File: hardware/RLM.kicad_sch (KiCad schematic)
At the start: 12 parts, among them U6 AP1117-33

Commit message: feat: add GY-521 footprint
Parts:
- U5: footprint (none) -> GRC:MicroSD-Module
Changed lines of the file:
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@@
       (effects (font (size 1.27 1.27)))
     )
-    (property "Footprint" "" (at 161.29 83.82 0)
+    (property "Footprint" "GRC:MicroSD-Module" (at 161.29 83.82 0)
       (effects (font (size 1.27 1.27)) hide)
     )

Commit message: chore: reorganize schematic
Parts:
- renumbered U6 to U3, U3 to U4, U4 to U5, U5 to U6
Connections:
- net +3.3V: no longer U6.2 (VCC)
- net +5V: now also U6.2 (VCC)
- net BN_RX: no longer U1.22 (TX2)
- net BN_TX: no longer U1.21 (RX2)
- net GY_SCL: no longer U1.29 (D22)
- net GY_SDA: no longer U1.26 (D21)
- net NRF_CE: no longer U1.20 (D4)
- net NRF_CSN: no longer U1.23 (D5)
- net NRF_MISO: no longer U1.25 (D19)
- net NRF_MOSI: no longer U1.30 (D23)
- net NRF_SCK: no longer U1.24 (D18)
- no-connect marks 8 -> 5
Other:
- note added: "Accelerometer/Gyroscope"
- note added: "ESP32 Pin Connections:"
- note added: "GPS"
- note added: "IMPORTANT: Before tracing, must finalize ESP32 pin connections TODO: - 2x 3-pin MOLEX - +5V, GND, V_sense - CAN_H, CAN_L, GND - CAN transciever"
- note added: "MicroSD Module"
- note added: "Microcontroller"
- note added: "Radio Module"
- note added: "Voltage Regulator"
- title: (none) -> Remote Logging Module
- moved on the sheet: C1, C2, C3, C4, D1, R1, U1, U2, U3, U4, U5, U6

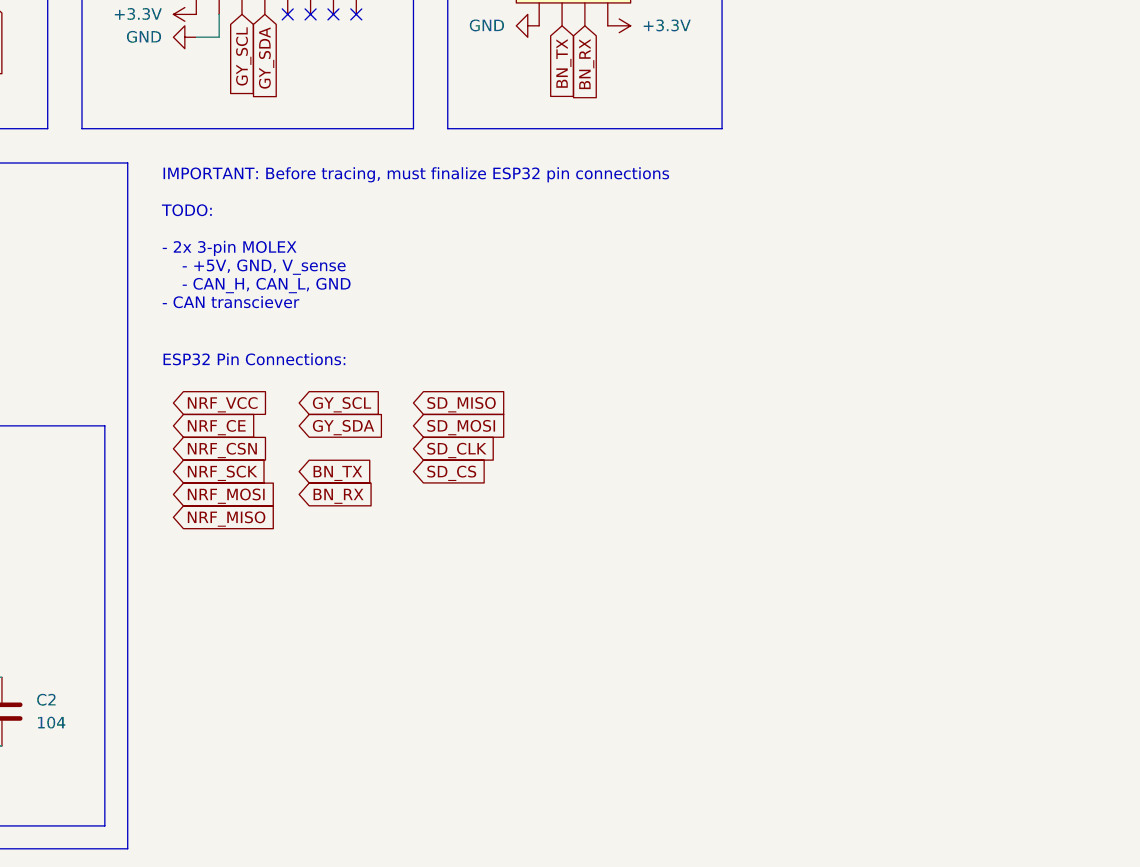
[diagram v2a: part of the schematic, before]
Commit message: feat: add CAN transceiver
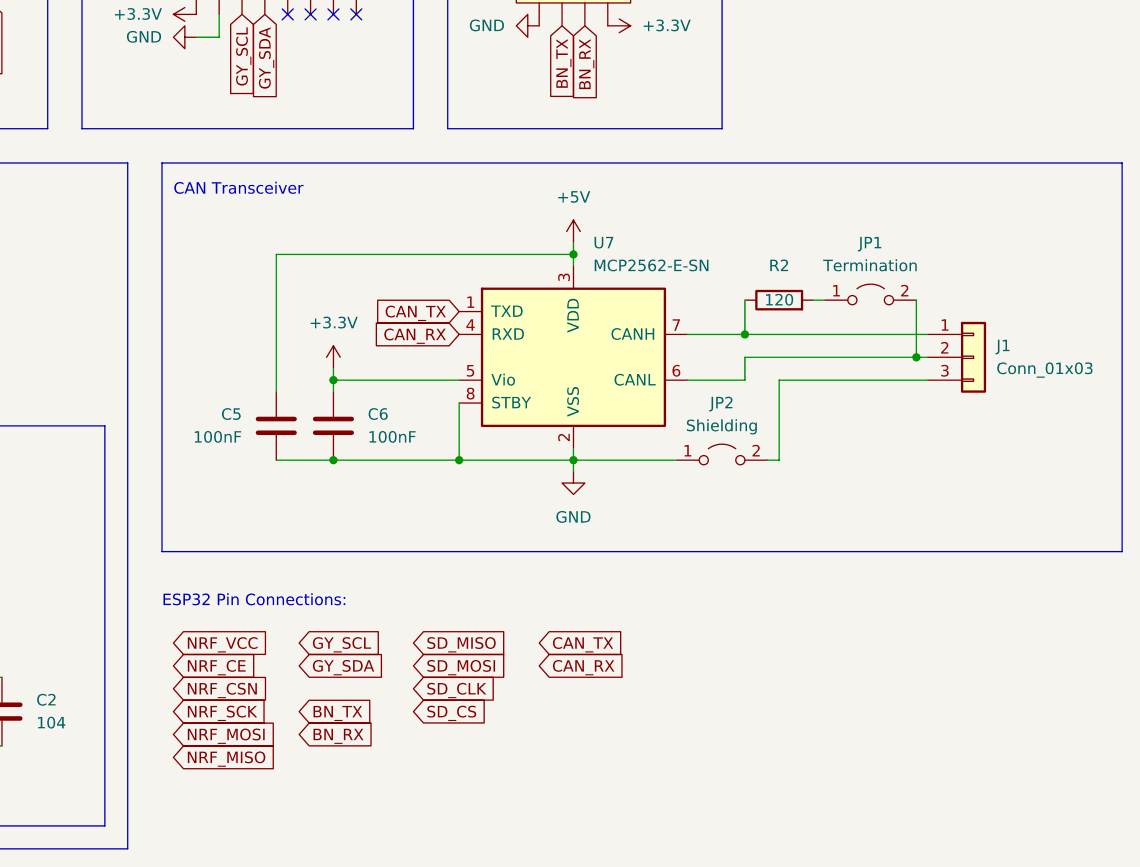
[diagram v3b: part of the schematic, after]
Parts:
- added C5, C6: 100nF, Capacitor_SMD:C_0603_1608Metric, symbol Device:C
- added J1: Conn_01x03, Connector_Molex:Molex_Micro-Fit_3.0_43650-0315_1x03_P3.00mm_Vertical, symbol Connector_Generic:Conn_01x03
- added JP1: Termination, Connector_PinHeader_2.54mm:PinHeader_1x02_P2.54mm_Vertical, symbol Jumper:Jumper_2_Open
- added JP2: Shielding, Connector_PinHeader_2.54mm:PinHeader_1x02_P2.54mm_Vertical, symbol Jumper:Jumper_2_Open
- added R2: 120, Resistor_SMD:R_0603_1608Metric, symbol Device:R
- added U7: MCP2562-E-SN, Package_SO:SOIC-8_3.9x4.9mm_P1.27mm, symbol Interface_CAN_LIN:MCP2562-E-SN
- C1, C2, C3, C4: footprint Capacitor_SMD:C_0603_1608Metric_Pad1.08x0.95mm_HandSolder -> Capacitor_SMD:C_0603_1608Metric
- D1: footprint LED_SMD:LED_0603_1608Metric_Pad1.05x0.95mm_HandSolder -> LED_SMD:LED_0603_1608Metric
- R1: footprint Resistor_SMD:R_0603_1608Metric_Pad0.98x0.95mm_HandSolder -> Resistor_SMD:R_0603_1608Metric
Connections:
- net +5V: now also C5.1, U7.3 (VDD)
- net GND: now also C5.2, C6.2, JP2.1 (A), U7.2 (VSS), U7.8 (STBY)
- new net: JP1.1 (A), R2.2
- new net: J1.2 (Pin_2), JP1.2 (B), U7.6 (CANL)
- new net: J1.1 (Pin_1), R2.1, U7.7 (CANH)
- new net: J1.3 (Pin_3), JP2.2 (B)
- new net CAN_RX: U7.4 (RXD)
- new net CAN_TX: U7.1 (TXD)
- new net GLV+: C6.1, U7.5 (Vio)
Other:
- note added: "CAN Transceiver"
- note removed: "IMPORTANT: Before tracing, must finalize ESP32 pin connections TODO: - 2x 3-pin MOLEX - +5V, GND, V_sense - CAN_H, CAN_L, GND - CAN transciever"

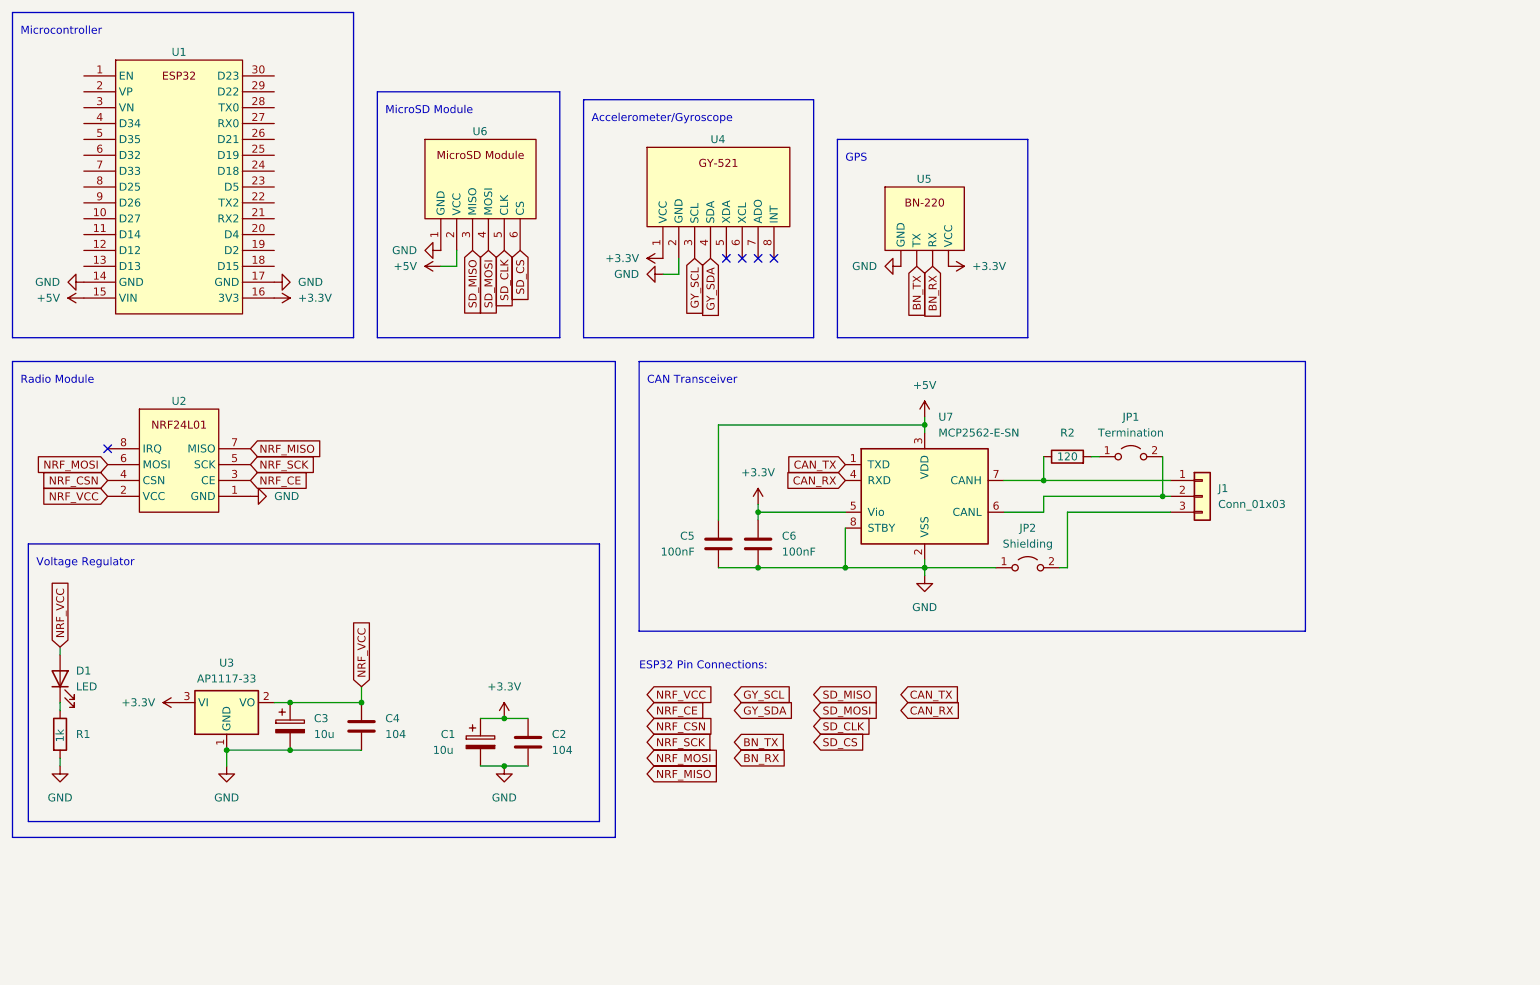
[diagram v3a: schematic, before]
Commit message: feat: add ESP32 power input
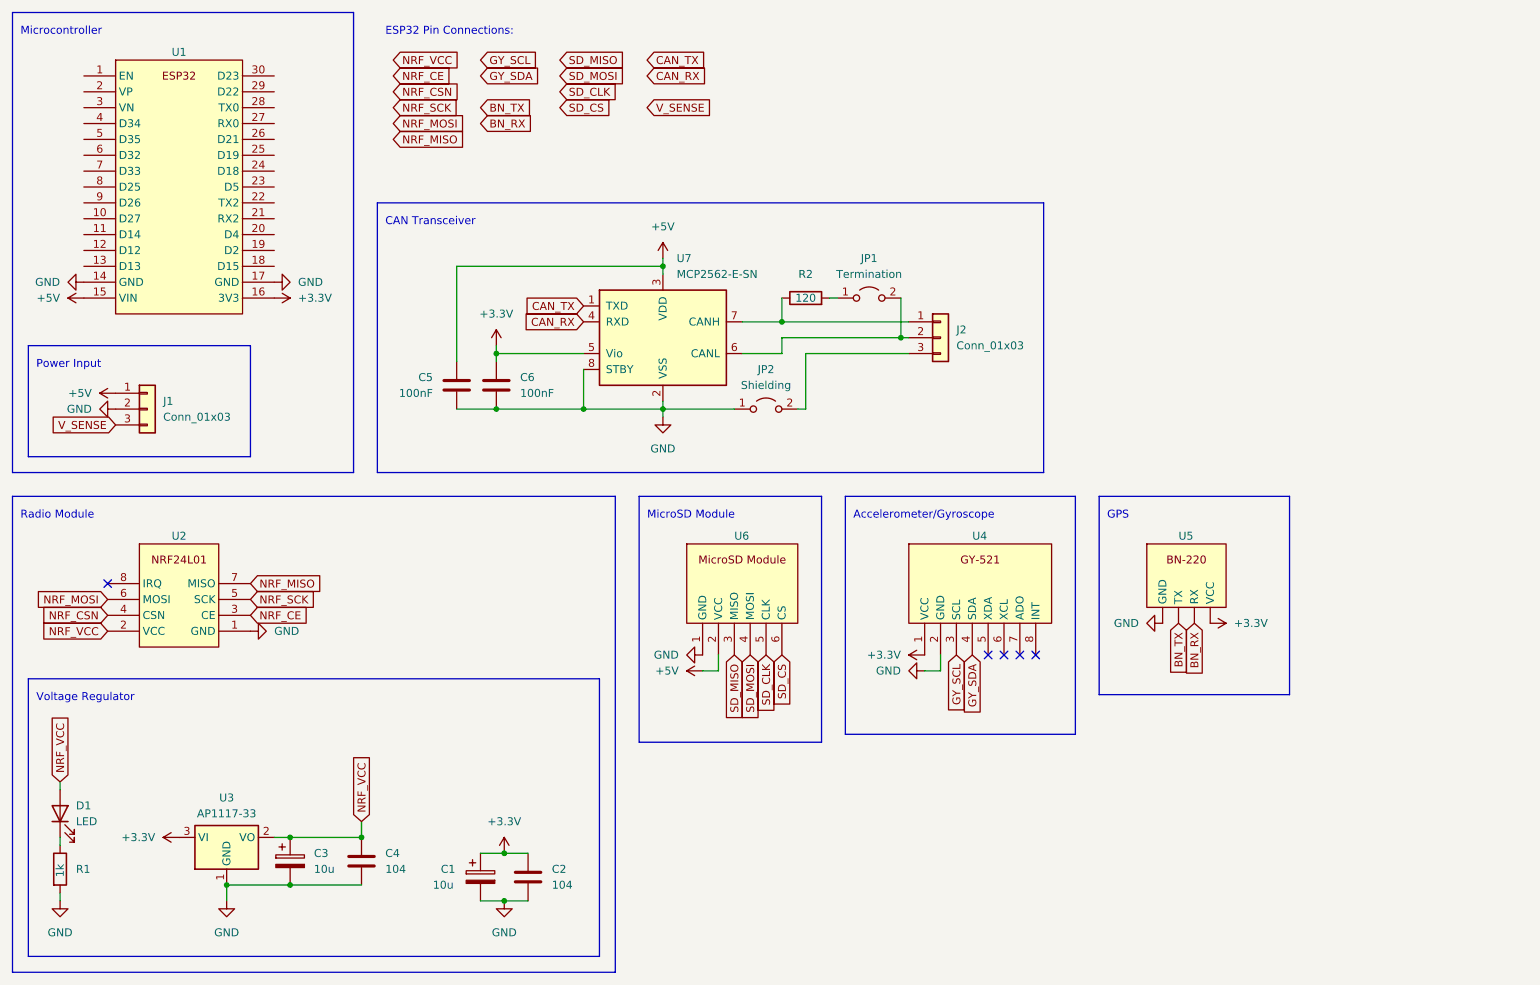
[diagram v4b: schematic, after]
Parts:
- added J1: Conn_01x03, Connector_Molex:Molex_Micro-Fit_3.0_43650-0315_1x03_P3.00mm_Vertical, symbol Connector_Generic:Conn_01x03
- renumbered J1 to J2
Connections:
- net +5V: now also J1.1 (Pin_1)
- net GND: now also J1.2 (Pin_2)
- new net V_SENSE: J1.3 (Pin_3)
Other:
- note added: "Power Input"
- moved on the sheet: C1, C2, C3, C4, C5, C6, D1, J2, JP1, JP2, R1, R2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

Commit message: chore: update ESP32 pin locations
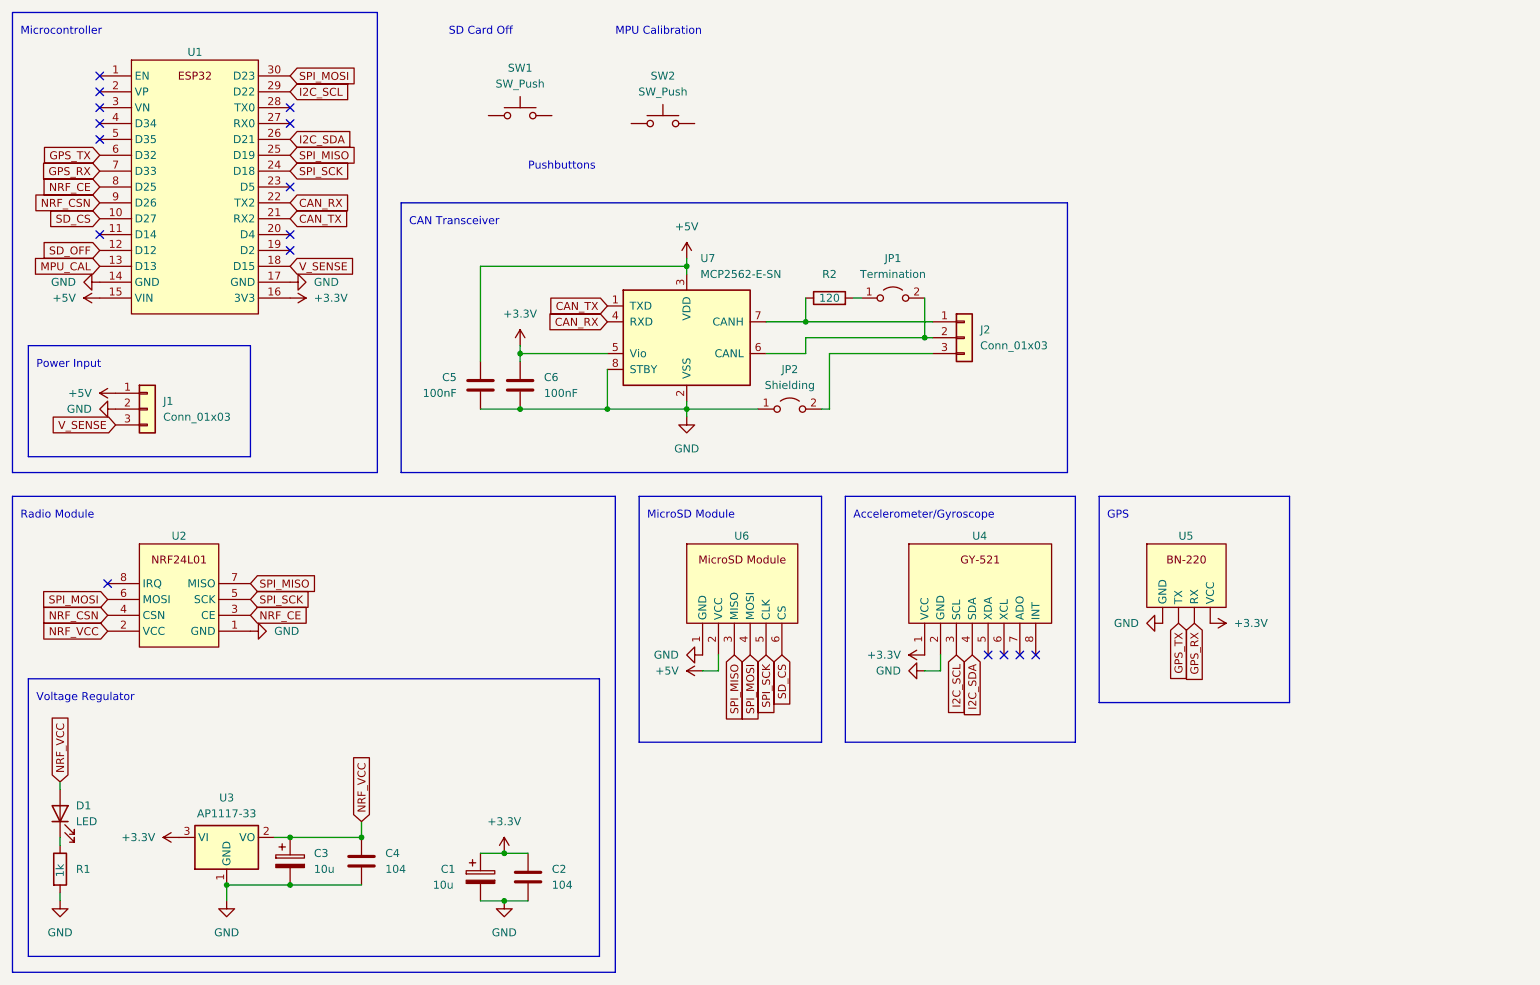
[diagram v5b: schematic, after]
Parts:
- added SW1, SW2: SW_Push, Button_Switch_THT:SW_PUSH_6mm, symbol Switch:SW_Push
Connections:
- net BN_RX is gone; now on net GPS_TX: U5. (VCC)
- net BN_TX is gone; now on net GPS_TX: U5. (VCC)
- net GY_SCL is gone; now on net I2C_SCL: U4.3 (SCL)
- net GY_SDA is gone; now on net I2C_SDA: U4.4 (SDA)
- net NRF_MISO is gone; now on net SPI_MISO: U2.7 (MISO)
- net NRF_MOSI is gone; now on net SPI_MOSI: U2.6 (MOSI)
- net NRF_SCK is gone; now on net SPI_SCK: U2.5 (SCK)
- net SD_CLK is gone; now on net SPI_SCK: U6.5 (CLK)
- net SD_MISO is gone; now on net SPI_MISO: U6.3 (MISO)
- net SD_MOSI is gone; now on net SPI_MOSI: U6.4 (MOSI)
- net CAN_RX: now also U1.22 (TX2)
- net CAN_TX: now also U1.21 (RX2)
- net NRF_CE: now also U1.8 (D25)
- net NRF_CSN: now also U1.9 (D26)
- net SD_CS: now also U1.10 (D27)
- net V_SENSE: now also U1.18 (D15)
- net SD_OFF: now reaches U1.12 (D12)
- net MPU_CAL: now reaches U1.13 (D13)
- net SPI_SCK: now reaches U1.24 (D18)
- net SPI_MISO: now reaches U1.25 (D19)
- net I2C_SDA: now reaches U1.26 (D21)
- net I2C_SCL: now reaches U1.29 (D22)
- net SPI_MOSI: now reaches U1.30 (D23)
- net GPS_TX: now reaches U1.6 (D32)
- net GPS_RX: now reaches U1.7 (D33)
- net GPS_RX: now also U5. (VCC)
- no-connect marks 5 -> 16
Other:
- note added: "MPU Calibration"
- note added: "Pushbuttons"
- note added: "SD Card Off"
- note removed: "ESP32 Pin Connections:"
- moved on the sheet: C5, C6, J2, JP1, JP2, R2, U1, U7

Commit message: feat: add pushbuttons
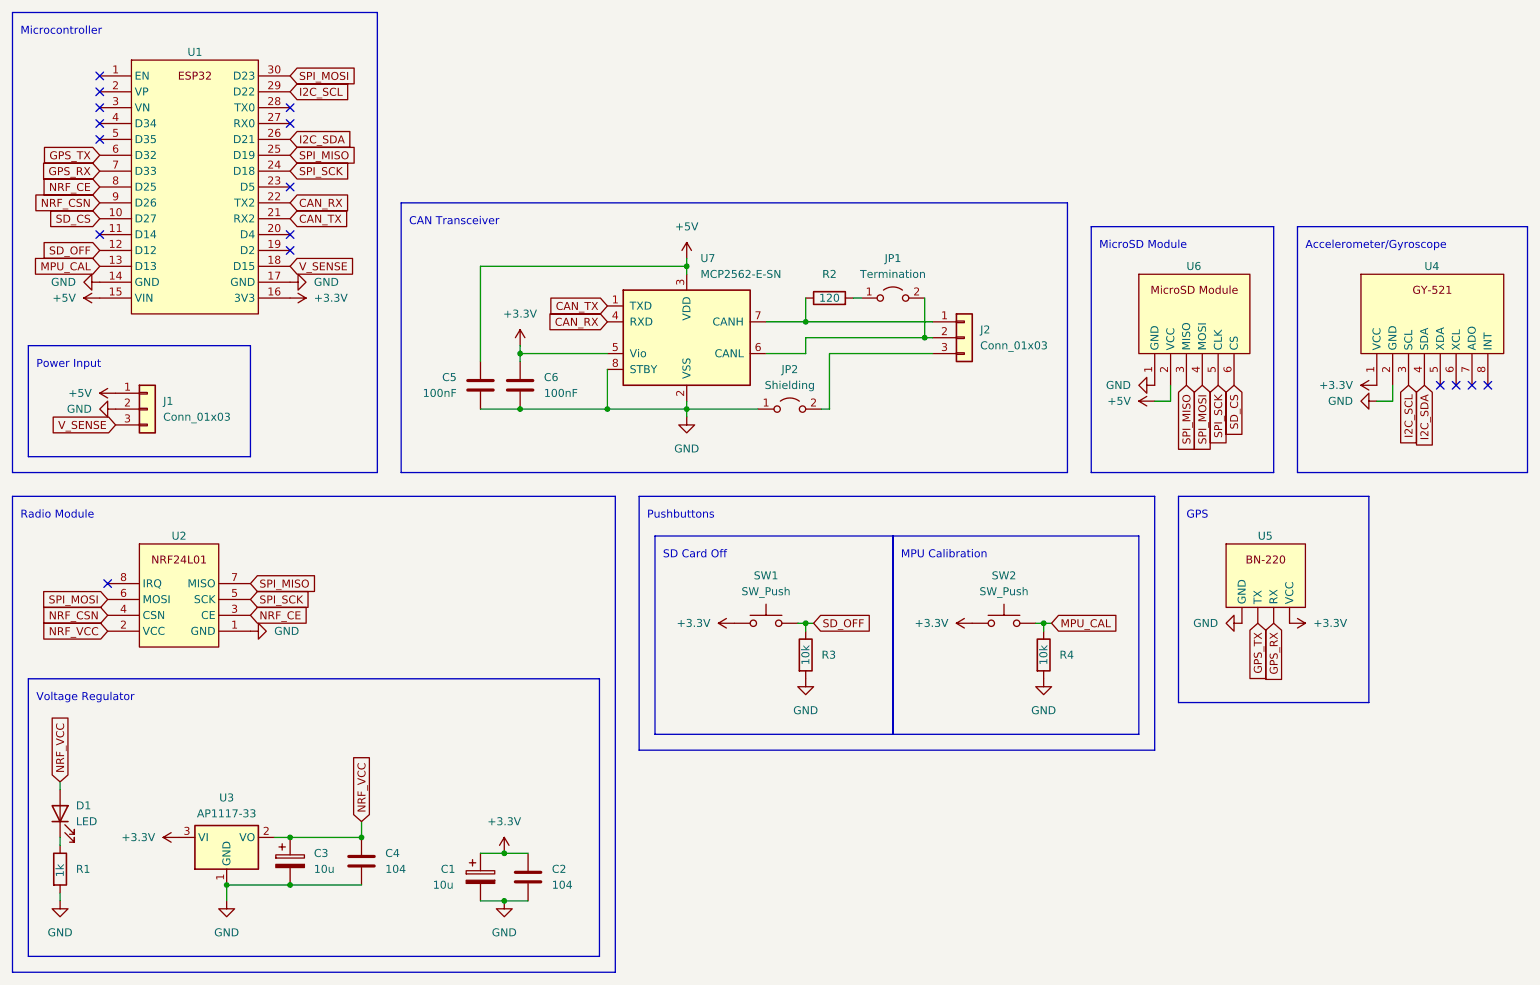
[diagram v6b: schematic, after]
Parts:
- added R3, R4: 10k, symbol Device:R
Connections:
- net +3.3V: now also SW1.1, SW2.1
- net GND: now also R3.2, R4.2
- net MPU_CAL: now also SW2.2, R4.1
- net SD_OFF: now also SW1.2, R3.1
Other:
- moved on the sheet: SW1, SW2, U4, U5, U6
